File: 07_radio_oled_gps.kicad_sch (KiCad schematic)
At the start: 26 parts, among them J40 Amphenol MDT420E01001 E-key W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, J41 SSD1306 OLED A 4-pin GND/VDD/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, J45 SSD1306 OLED B 4-pin GND/VDD/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, U170 SN74LVC3G34DCUR E-key control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, U45 TCA9548A service I2C mux @0x70

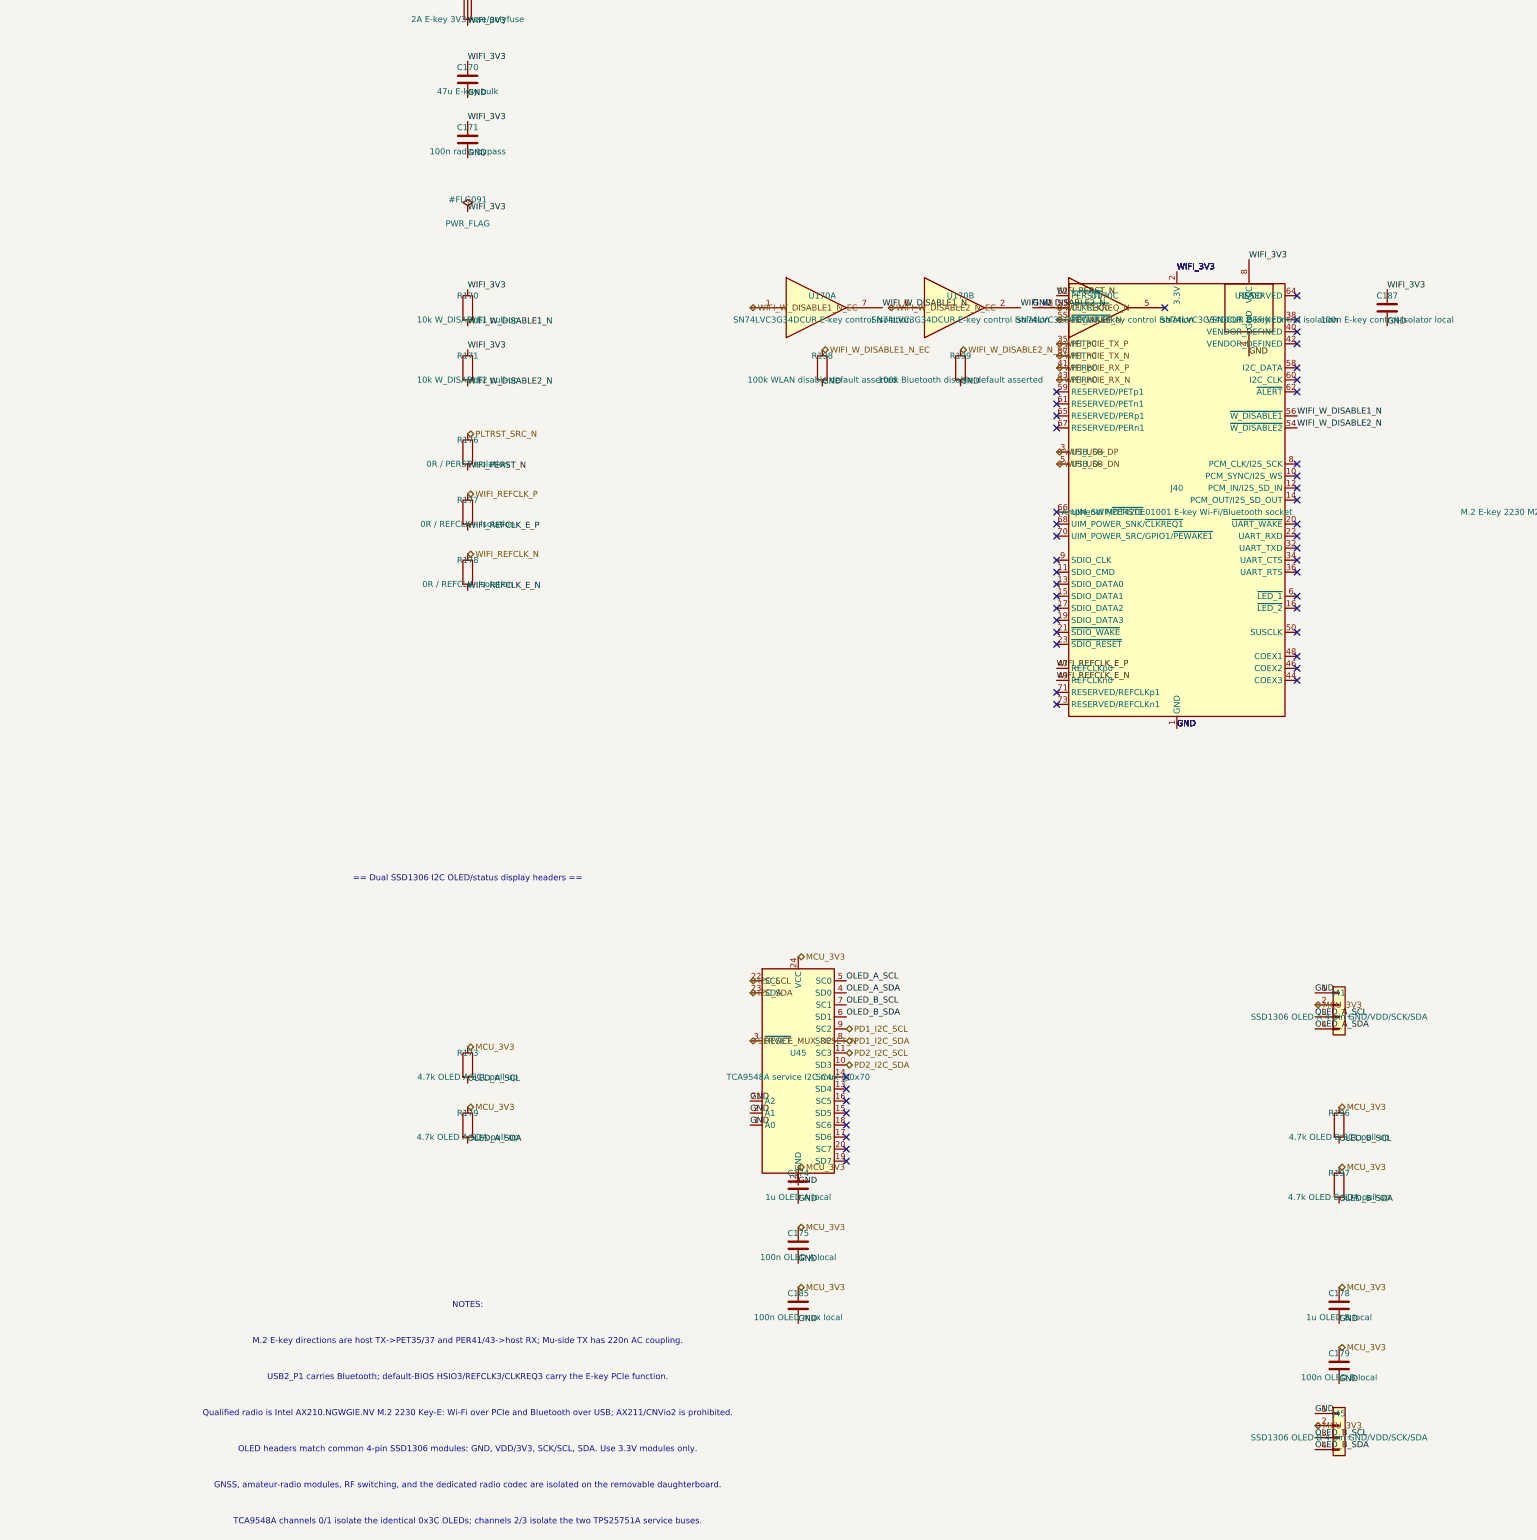
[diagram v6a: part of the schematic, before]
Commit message: wire the oleds and clean up the center board
fix the hdmi 5v budget in the schematic and add the routing rules. the right pcb sync and remaining placement work are still next.
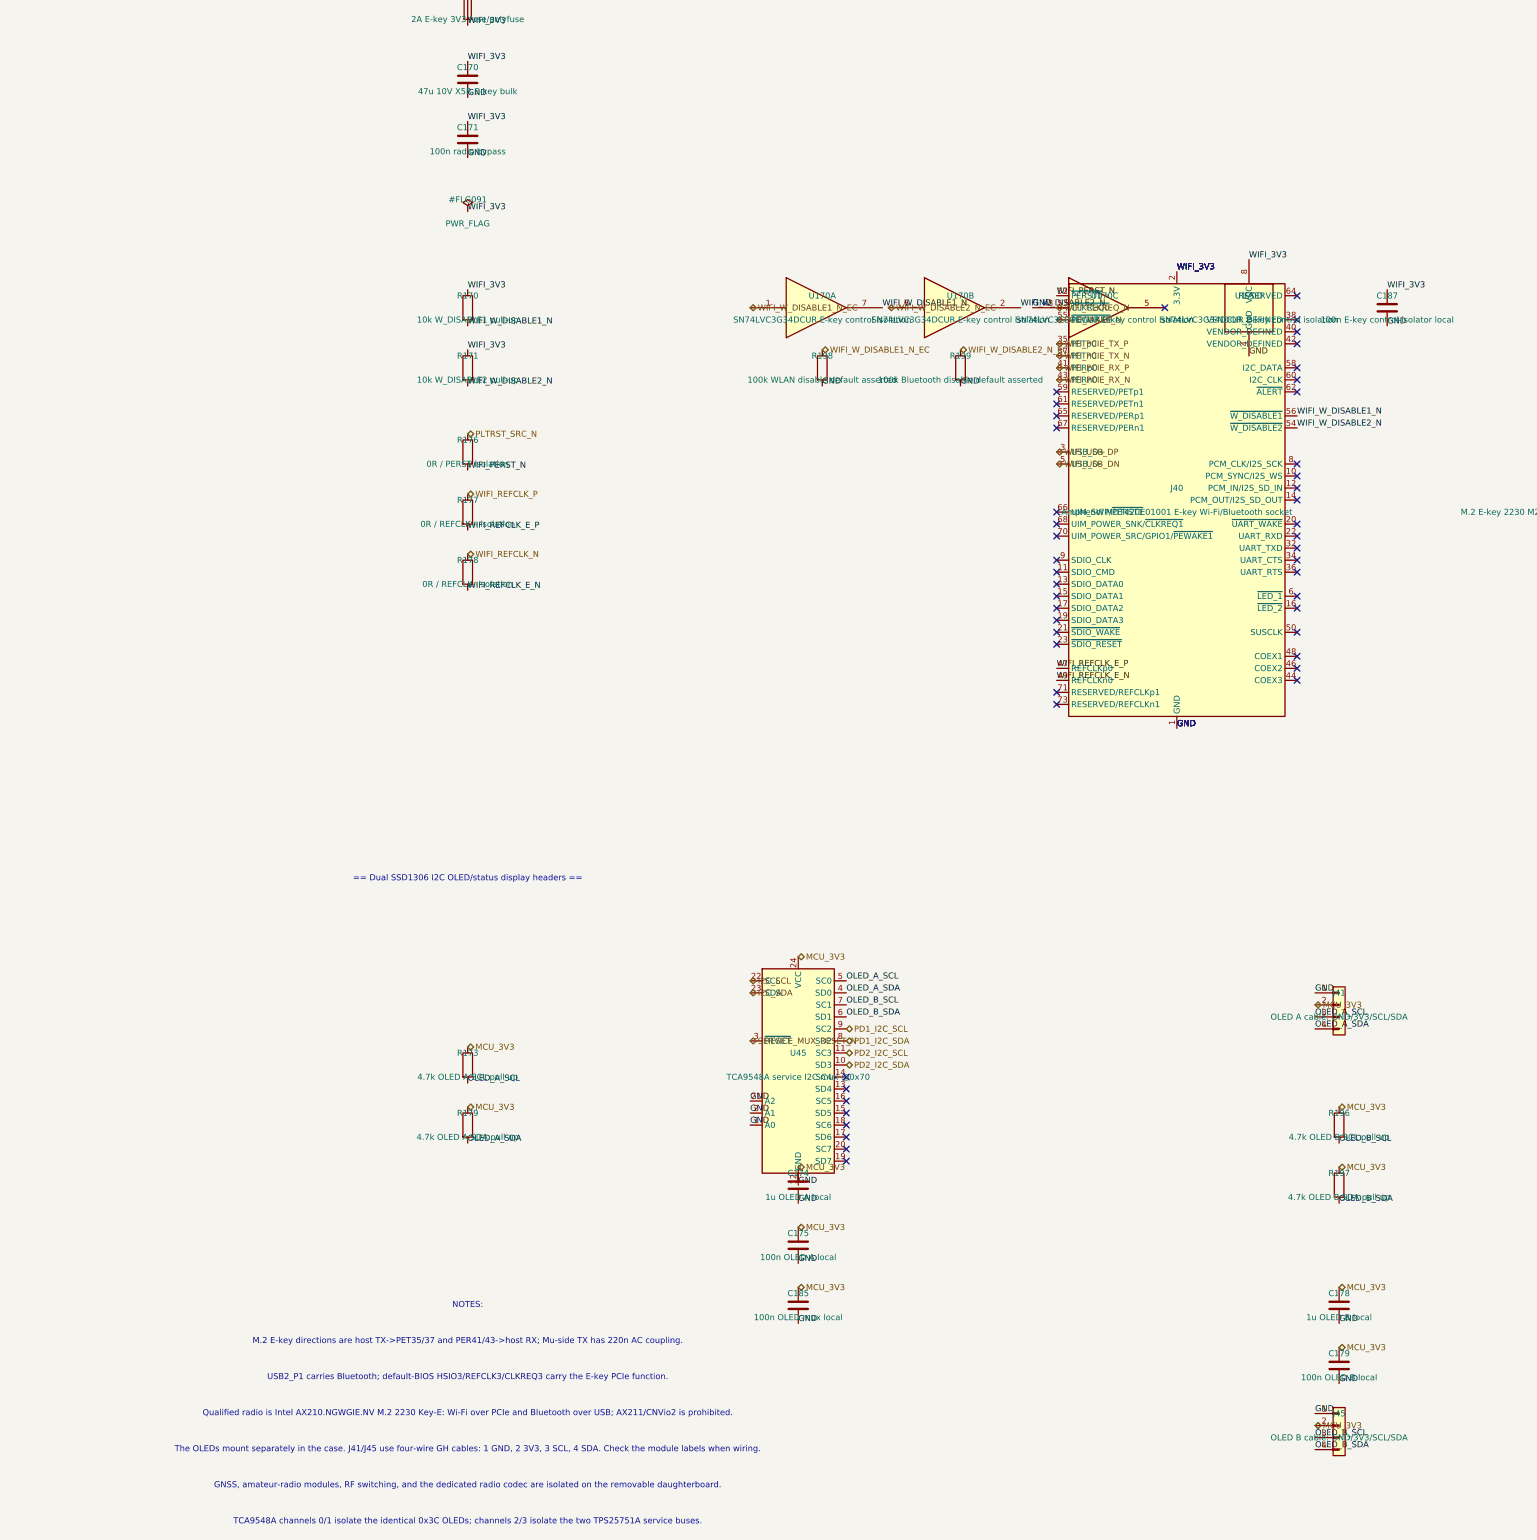
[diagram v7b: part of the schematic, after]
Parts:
- C170: value 47u E-key bulk -> 47u 10V X5R E-key bulk; MPN GRM31CR71E106KA12L -> GRM31CR61A476ME15L
- J41: value SSD1306 OLED A 4-pin GND/VDD/SCK/SDA -> OLED A cable: GND/3V3/SCL/SDA; footprint ducktop2:SSD1306_0.96in_Module_4Pin -> Connector_JST:JST_GH_SM04B-GHS-TB_1x04-1MP_P1.25mm_Horizontal; AssemblyID OLED-A-SSD1306-0P96-4PIN-GND-VDD-SCK-SDA -> (none); CablePinout (none) -> 1=GND;2=3V3;3=SCL;4=SDA; Contacts (none) -> SSHL-002T-P0.2; Endpoint (none) -> OLED A, mounted separately in the case; MPN (none) -> SM04B-GHS-TB; Manufacturer (none) -> JST; MatingHousing (none) -> GHR-04V-S; MechanicalEnvelope 27.0x27.0mm module; verify owned sample before enclosure re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 -> (none); ProcurementClass Owner-supplied measured module -> (none)
- J45: value SSD1306 OLED B 4-pin GND/VDD/SCK/SDA -> OLED B cable: GND/3V3/SCL/SDA; footprint ducktop2:SSD1306_0.96in_Module_4Pin -> Connector_JST:JST_GH_SM04B-GHS-TB_1x04-1MP_P1.25mm_Horizontal; AssemblyID OLED-B-SSD1306-0P96-4PIN-GND-VDD-SCK-SDA -> (none); CablePinout (none) -> 1=GND;2=3V3;3=SCL;4=SDA; Contacts (none) -> SSHL-002T-P0.2; Endpoint (none) -> OLED B, mounted separately in the case; MPN (none) -> SM04B-GHS-TB; Manufacturer (none) -> JST; MatingHousing (none) -> GHR-04V-S; MechanicalEnvelope 27.0x27.0mm module; verify owned sample before enclosure re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 -> (none); ProcurementClass Owner-supplied measured module -> (none)
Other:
- note added: "The OLEDs mount separately in the case. J41/J45 use four-wire GH cables: 1 GND, 2 3V3, 3 SCL, 4 SDA. Check the module labels when wiring."
- note removed: "OLED headers match common 4-pin SSD1306 modules: GND, VDD/3V3, SCK/SCL, SDA. Use 3.3V modules only."
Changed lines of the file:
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@@
   (dnp no)
   (property "Reference" "C170" (at 20.32 88.9 0) (effects (font (size 1.27 1.27))))
-  (property "Value" "47u E-key bulk" (at 20.32 93.98 0) (effects (font (size 1.27 1.27))))
+  (property "Value" "47u 10V X5R E-key bulk" (at 20.32 93.98 0) (effects (font (size 1.27 1.27))))
   (property "Footprint" "Capacitor_SMD:C_1206_3216Metric" (at 20.32 91.44 0) (effects (font (size 1.27 1.27)) (hide yes)))
   (property "Datasheet" "" (at 20.32 91.44 0) (effects (font (size 1.27 1.27)) (hide yes)))
   (property "Manufacturer" "Murata" (at 20.32 91.44 0) (effects (font (size 1.27 1.27)) (hide yes)))
-  (property "MPN" "GRM31CR71E106KA12L" (at 20.32 91.44 0) (effects (font (size 1.27 1.27)) (hide yes)))
+  (property "MPN" "GRM31CR61A476ME15L" (at 20.32 91.44 0) (effects (font (size 1.27 1.27)) (hide yes)))
   (pin "1")
   (pin "2")
@@
   (dnp no)
   (property "Reference" "J41" (at 204.47 284.48 0) (effects (font (size 1.27 1.27))))
-  (property "Value" "SSD1306 OLED A 4-pin GND/VDD/SCK/SDA" (at 204.47 289.56 0) (effects (font (size 1.27 1.27))))
-  (property "Footprint" "ducktop2:SSD1306_0.96in_Module_4Pin" (at 204.47 287.02 0) (effects (font (size 1.27 1.27)) (hide yes)))
+  (property "Value" "OLED A cable: GND/3V3/SCL/SDA" (at 204.47 289.56 0) (effects (font (size 1.27 1.27))))
+  (property "Footprint" "Connector_JST:JST_GH_SM04B-GHS-TB_1x04-1MP_P1.25mm_Horizontal" (at 204.47 287.02 0) (effects (font (size 1.27 1.27)) (hide yes)))
   (property "Datasheet" "" (at 204.47 287.02 0) (effects (font (size 1.27 1.27)) (hide yes)))
-  (property "ProcurementClass" "Owner-supplied measured module" (at 204.47 287.02 0) (effects (font (size 1.27 1.27)) (hide yes)))
-  (property "AssemblyID" "OLED-A-SSD1306-0P96-4PIN-GND-VDD-SCK-SDA" (at 204.47 287.02 0) (effects (font (size 1.27 1.27)) (hide yes)))
-  (property "MechanicalEnvelope" "27.0x27.0mm module; verify owned sample before enclosure release" (at 204.47 287.02 0) (effects (font (size 1.27 1.27)) (hide yes)))
+  (property "Manufacturer" "JST" (at 204.47 287.02 0) (effects (font (size 1.27 1.27)) (hide yes)))
+  (property "MPN" "SM04B-GHS-TB" (at 204.47 287.02 0) (effects (font (size 1.27 1.27)) (hide yes)))
+  (property "MatingHousing" "GHR-04V-S" (at 204.47 287.02 0) (effects (font (size 1.27 1.27)) (hide yes)))
+  (property "Contacts" "SSHL-002T-P0.2" (at 204.47 287.02 0) (effects (font (size 1.27 1.27)) (hide yes)))
+  (property "Endpoint" "OLED A, mounted separately in the case" (at 204.47 287.02 0) (effects (font (size 1.27 1.27)) (hide yes)))
+  (property "CablePinout" "1=GND;2=3V3;3=SCL;4=SDA" (at 204.47 287.02 0) (effects (font (size 1.27 1.27)) (hide yes)))
   (pin "1")
   (pin "2")
@@
   (dnp no)
   (property "Reference" "J45" (at 204.47 373.38 0) (effects (font (size 1.27 1.27))))
-  (property "Value" "SSD1306 OLED B 4-pin GND/VDD/SCK/SDA" (at 204.47 378.46 0) (effects (font (size 1.27 1.27))))
-  (property "Footprint" "ducktop2:SSD1306_0.96in_Module_4Pin" (at 204.47 375.92 0) (effects (font (size 1.27 1.27)) (hide yes)))
+  (property "Value" "OLED B cable: GND/3V3/SCL/SDA" (at 204.47 378.46 0) (effects (font (size 1.27 1.27))))
+  (property "Footprint" "Connector_JST:JST_GH_SM04B-GHS-TB_1x04-1MP_P1.25mm_Horizontal" (at 204.47 375.92 0) (effects (font (size 1.27 1.27)) (hide yes)))
   (property "Datasheet" "" (at 204.47 375.92 0) (effects (font (size 1.27 1.27)) (hide yes)))
-  (property "ProcurementClass" "Owner-supplied measured module" (at 204.47 375.92 0) (effects (font (size 1.27 1.27)) (hide yes)))
-  (property "AssemblyID" "OLED-B-SSD1306-0P96-4PIN-GND-VDD-SCK-SDA" (at 204.47 375.92 0) (effects (font (size 1.27 1.27)) (hide yes)))
-  (property "MechanicalEnvelope" "27.0x27.0mm module; verify owned sample before enclosure release" (at 204.47 375.92 0) (effects (font (size 1.27 1.27)) (hide yes)))
+  (property "Manufacturer" "JST" (at 204.47 375.92 0) (effects (font (size 1.27 1.27)) (hide yes)))
+  (property "MPN" "SM04B-GHS-TB" (at 204.47 375.92 0) (effects (font (size 1.27 1.27)) (hide yes)))
+  (property "MatingHousing" "GHR-04V-S" (at 204.47 375.92 0) (effects (font (size 1.27 1.27)) (hide yes)))
+  (property "Contacts" "SSHL-002T-P0.2" (at 204.47 375.92 0) (effects (font (size 1.27 1.27)) (hide yes)))
+  (property "Endpoint" "OLED B, mounted separately in the case" (at 204.47 375.92 0) (effects (font (size 1.27 1.27)) (hide yes)))
+  (property "CablePinout" "1=GND;2=3V3;3=SCL;4=SDA" (at 204.47 375.92 0) (effects (font (size 1.27 1.27)) (hide yes)))
   (pin "1")
   (pin "2")
@@
 (text "USB2_P1 carries Bluetooth; default-BIOS HSIO3/REFCLK3/CLKREQ3 carry the E-key PCIe function." (at 20.32 365.76 0) (effects (font (size 1.27 1.27))))
 (text "Qualified radio is Intel AX210.NGWGIE.NV M.2 2230 Key-E: Wi-Fi over PCIe and Bluetooth over USB; AX211/CNVio2 is prohibited." (at 20.32 373.38 0) (effects (font (size 1.27 1.27))))
-(text "OLED headers match common 4-pin SSD1306 modules: GND, VDD/3V3, SCK/SCL, SDA. Use 3.3V modules only." (at 20.32 381 0) (effects (font (size 1.27 1.27))))
+(text "The OLEDs mount separately in the case. J41/J45 use four-wire GH cables: 1 GND, 2 3V3, 3 SCL, 4 SDA. Check the module labels when wiring." (at 20.32 381 0) (effects (font (size 1.27 1.27))))
 (text "GNSS, amateur-radio modules, RF switching, and the dedicated radio codec are isolated on the removable daughterboard." (at 20.32 388.62 0) (effects (font (size 1.27 1.27))))
 (text "TCA9548A channels 0/1 isolate the identical 0x3C OLEDs; channels 2/3 isolate the two TPS25751A service buses." (at 20.32 396.24 0) (effects (font (size 1.27 1.27))))
